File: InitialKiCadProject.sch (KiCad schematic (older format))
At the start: 0 parts

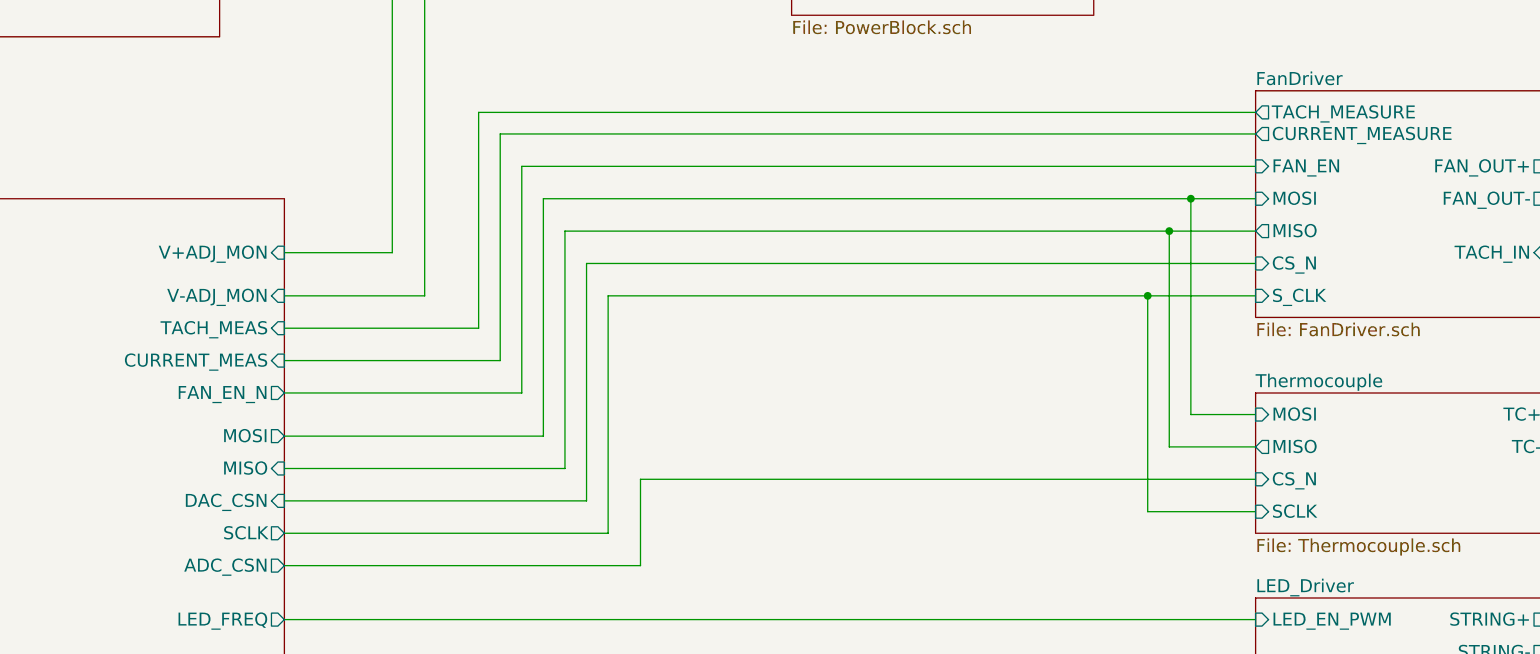
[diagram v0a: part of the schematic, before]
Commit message: Fan/Current mode redo
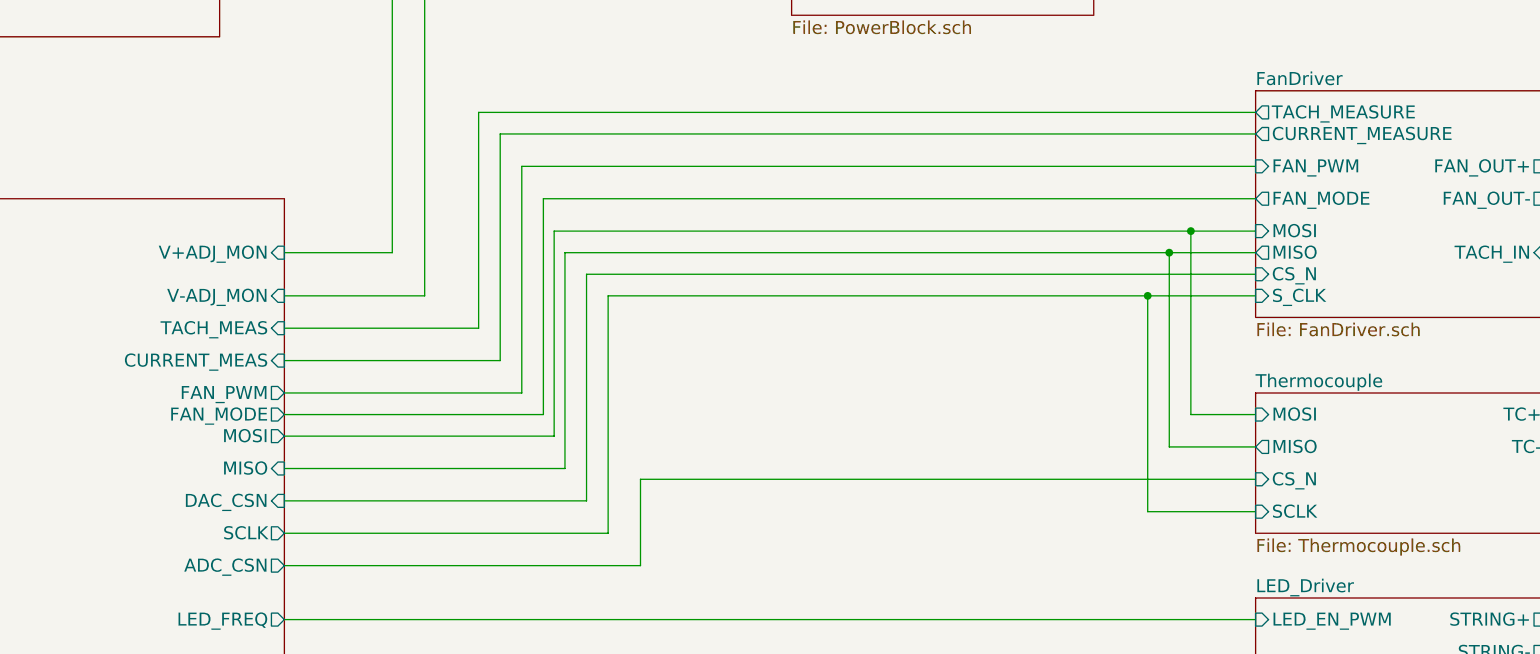
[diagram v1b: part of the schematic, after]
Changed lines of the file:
@@
-EESchema Schematic File Version 2  date Sat 08 Feb 2014 11:37:49 PM EST
+EESchema Schematic File Version 2  date Sun 09 Feb 2014 12:22:09 AM EST
 LIBS:power
 LIBS:device
@@
 Comment4 ""
 $EndDescr
+Connection ~ 8150 3200
+Wire Wire Line
+	8150 3200 8150 4100
+Wire Wire Line
+	8550 3300 5450 3300
+Wire Wire Line
+	5450 3300 5450 4350
+Wire Wire Line
+	8550 3100 5300 3100
+Wire Wire Line
+	5300 3100 5300 4050
+Wire Wire Line
+	5300 4050 4050 4050
 Wire Wire Line
 	9900 3200 10200 3200
@@
 Wire Wire Line
 	8050 4400 8550 4400
-Connection ~ 8250 2950
-Wire Wire Line
-	8250 2950 8250 3950
-Wire Wire Line
-	8250 3950 8550 3950
-Wire Wire Line
-	8550 3250 5450 3250
-Wire Wire Line
-	5450 3250 5450 4350
+Wire Wire Line
+	8550 3950 8250 3950
 Wire Wire Line
 	5450 4350 4050 4350
@@
 	8550 2950 5250 2950
 Wire Wire Line
-	5250 2950 5250 4050
-Wire Wire Line
-	5250 4050 4050 4050
-Wire Wire Line
 	4050 3700 5050 3700
 Wire Wire Line
@@
 	4050 4200 5350 4200
 Wire Wire Line
-	5350 4200 5350 3100
-Wire Wire Line
-	5350 3100 8550 3100
-Wire Wire Line
 	5550 4500 5550 3400
 Wire Wire Line
 	5550 3400 8550 3400
 Wire Wire Line
-	8550 4100 8150 4100
-Wire Wire Line
-	8150 4100 8150 3100
-Connection ~ 8150 3100
+	8150 4100 8550 4100
 Wire Wire Line
 	4050 4650 5700 4650
@@
 Wire Wire Line
 	9900 2950 10200 2950
+Wire Wire Line
+	4050 3950 5250 3950
+Wire Wire Line
+	5250 3950 5250 2950
+Wire Wire Line
+	5350 4200 5350 3200
+Wire Wire Line
+	5350 3200 8550 3200
+Wire Wire Line
+	8250 3950 8250 3100
+Connection ~ 8250 3100
 $Sheet
 S 8550 3850 1400 650
@@
 F1 "FanDriver.sch" 60
 F2 "FAN_OUT+" O R 9900 2800 60
-F3 "FAN_EN" I L 8550 2800 60
-F4 "TACH_MEASURE" O L 8550 2550 60
-F5 "TACH_IN" I R 9900 3200 60
-F6 "CURRENT_MEASURE" O L 8550 2650 60
-F7 "MISO" O L 8550 3100 60
-F8 "MOSI" I L 8550 2950 60
-F9 "CS_N" I L 8550 3250 60
-F10 "S_CLK" I L 8550 3400 60
-F11 "FAN_OUT-" O R 9900 2950 60
+F3 "TACH_MEASURE" O L 8550 2550 60
+F4 "TACH_IN" I R 9900 3200 60
+F5 "CURRENT_MEASURE" O L 8550 2650 60
+F6 "MISO" O L 8550 3200 60
+F7 "MOSI" I L 8550 3100 60
+F8 "CS_N" I L 8550 3300 60
+F9 "S_CLK" I L 8550 3400 60
+F10 "FAN_OUT-" O R 9900 2950 60
+F11 "FAN_MODE" O L 8550 2950 60
+F12 "FAN_PWM" I L 8550 2800 60
 $EndSheet
 $Sheet
@@
 F7 "CURRENT_MEAS" I R 4050 3700 60
 F8 "TACH_MEAS" I R 4050 3550 60
-F9 "FAN_EN_N" O R 4050 3850 60
-F10 "Relay-" O R 4050 5300 60
-F11 "V-ADJ_MON" I R 4050 3400 60
-F12 "V+ADJ_MON" I R 4050 3200 60
-F13 "DAC_CSN" I R 4050 4350 60
-F14 "ADC_CSN" O R 4050 4650 60
+F9 "Relay-" O R 4050 5300 60
+F10 "V-ADJ_MON" I R 4050 3400 60
+F11 "V+ADJ_MON" I R 4050 3200 60
+F12 "DAC_CSN" I R 4050 4350 60
+F13 "ADC_CSN" O R 4050 4650 60
+F14 "FAN_PWM" O R 4050 3850 60
+F15 "FAN_MODE" O R 4050 3950 60
 $EndSheet
 $Sheet
